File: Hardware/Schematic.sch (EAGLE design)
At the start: 14 parts, among them IC1 XC6220A331MR-G, J1 SAMACSYS_PARTS_USB4110-GF-A, Q1 20V/4.2A/52mΩ/1.4W

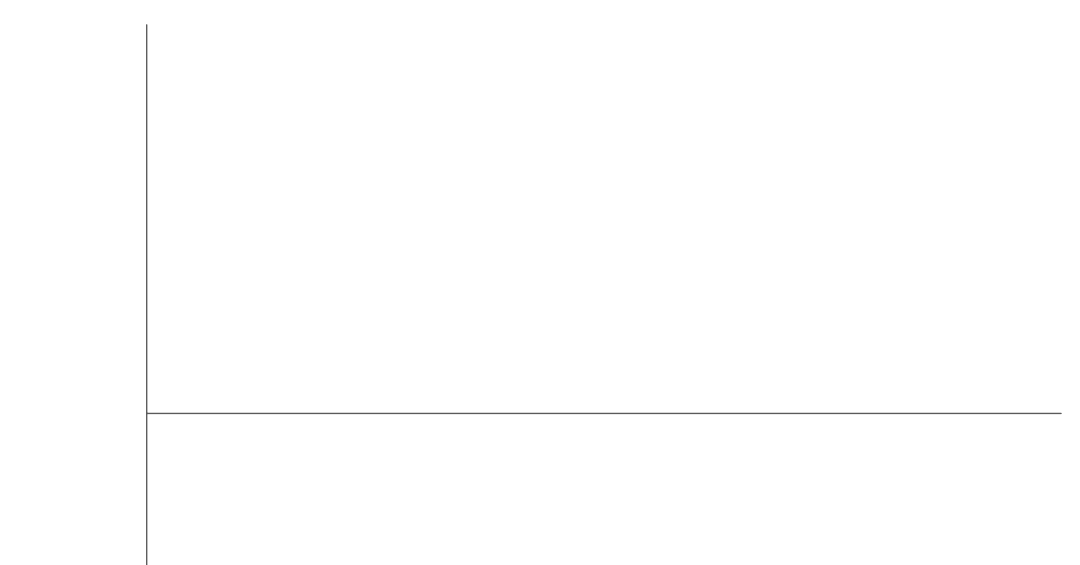
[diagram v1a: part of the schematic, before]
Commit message: add SD Card
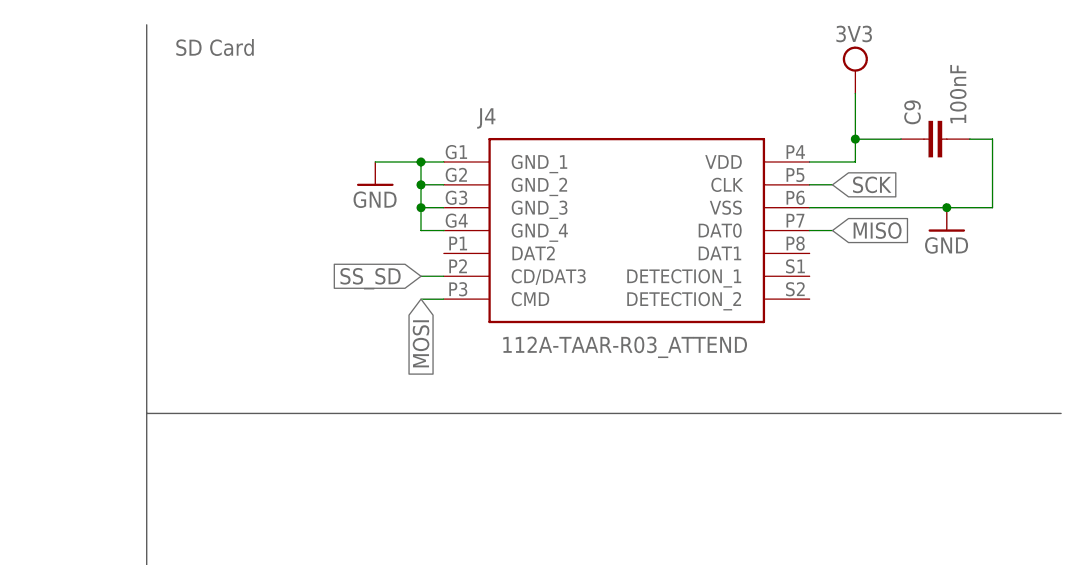
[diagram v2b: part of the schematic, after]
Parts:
- added C9: 100nF, DeskAssistant v19 v1.flbr:EAGLE-LTSPICE_CC0402
- added J4: 112A-TAAR-R03_ATTEND, DeskAssistant v19 v1.flbr:112A-TAAR-R03_ATTEND
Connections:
- new net MISO: J4.DAT0
- new net MOSI: J4.CMD
- new net SCK: J4.CLK
- new net SS_SD: J4.CD/DAT3
- net 3V3: now also C9.1, J4.VDD
- net GND: now also C9.2, J4.GND_1, J4.GND_2, J4.GND_3, J4.GND_4, J4.VSS
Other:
- note added: "SD Card"
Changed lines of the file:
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@@
 <part name="C1_BAT2" library="DeskAssistant v19 v1.flbr" library_urn="urn:adsk.wipprod:fs.file:vf.vVvdDOfaSfavM5thX5SjWw" deviceset="ESP32_WROVER_EAGLE-LTSPICE_C" device="C0402" value="4.7uF"/>
 <part name="C1_BAT1" library="DeskAssistant v19 v1.flbr" library_urn="urn:adsk.wipprod:fs.file:vf.vVvdDOfaSfavM5thX5SjWw" deviceset="ESP32_WROVER_EAGLE-LTSPICE_C" device="C0402" value="4.7uF"/>
+<part name="J4" library="DeskAssistant v19 v1.flbr" library_urn="urn:adsk.wipprod:fs.file:vf.vVvdDOfaSfavM5thX5SjWw" deviceset="112A-TAAR-R03_ATTEND" device=""/>
+<part name="GND11" library="DeskAssistant v19 v1.flbr" library_urn="urn:adsk.wipprod:fs.file:vf.vVvdDOfaSfavM5thX5SjWw" deviceset="GND" device=""/>
+<part name="GND12" library="DeskAssistant v19 v1.flbr" library_urn="urn:adsk.wipprod:fs.file:vf.vVvdDOfaSfavM5thX5SjWw" deviceset="GND" device=""/>
+<part name="C9" library="DeskAssistant v19 v1.flbr" library_urn="urn:adsk.wipprod:fs.file:vf.vVvdDOfaSfavM5thX5SjWw" deviceset="EAGLE-LTSPICE_C" device="C0402" value="100nF"/>
+<part name="SUPPLY2" library="DeskAssistant v19 v1.flbr" library_urn="urn:adsk.wipprod:fs.file:vf.vVvdDOfaSfavM5thX5SjWw" deviceset="3V3-CIRCLE" device="" value="3V3"/>
 </parts>
 <sheets>
@@
 ESD Protection</text>
 <text x="-2.54" y="271.78" size="1.778" layer="95" align="center">LDO Voltage Regulator</text>
+<text x="124.46" y="274.32" size="1.778" layer="95" align="center">SD Card</text>
 </plain>
 <instances>
@@
 <attribute name="NAME" x="23.876" y="235.839" size="1.778" layer="95" rot="R180"/>
 <attribute name="VALUE" x="23.876" y="240.919" size="1.778" layer="96" rot="R180"/>
+</instance>
+<instance part="J4" gate="G$1" x="149.86" y="261.62" smashed="yes">
+<attribute name="NAME" x="153.67" y="266.7" size="1.778" layer="95" align="center-left"/>
+<attribute name="VALUE" x="156.21" y="241.3" size="1.778" layer="96" align="center-left"/>
+</instance>
+<instance part="GND11" gate="1" x="142.24" y="259.08" smashed="yes">
+<attribute name="VALUE" x="139.7" y="256.54" size="1.778" layer="96"/>
+</instance>
+<instance part="GND12" gate="1" x="205.74" y="254" smashed="yes">
+<attribute name="VALUE" x="203.2" y="251.46" size="1.778" layer="96"/>
+</instance>
+<instance part="C9" gate="G$1" x="203.2" y="264.16" smashed="yes" rot="R90">
+<attribute name="NAME" x="202.819" y="265.684" size="1.778" layer="95" rot="R90"/>
+<attribute name="VALUE" x="207.899" y="265.684" size="1.778" layer="96" rot="R90"/>
+</instance>
+<instance part="SUPPLY2" gate="G$1" x="195.58" y="271.78" smashed="yes">
+<attribute name="VALUE" x="195.453" y="274.955" size="1.778" layer="96" align="bottom-center"/>
 </instance>
 </instances>
@@
 <pinref part="GND10" gate="1" pin="GND"/>
 </segment>
+<segment>
+<pinref part="J4" gate="G$1" pin="GND_4"/>
+<wire x1="149.86" y1="254" x2="147.32" y2="254" width="0.1524" layer="91"/>
+<wire x1="147.32" y1="254" x2="147.32" y2="256.54" width="0.1524" layer="91"/>
+<wire x1="147.32" y1="256.54" x2="147.32" y2="259.08" width="0.1524" layer="91"/>
+<wire x1="147.32" y1="259.08" x2="147.32" y2="261.62" width="0.1524" layer="91"/>
+<wire x1="147.32" y1="261.62" x2="149.86" y2="261.62" width="0.1524" layer="91"/>
+<pinref part="J4" gate="G$1" pin="GND_1"/>
+<pinref part="J4" gate="G$1" pin="GND_2"/>
+<wire x1="149.86" y1="259.08" x2="147.32" y2="259.08" width="0.1524" layer="91"/>
+<junction x="147.32" y="259.08"/>
+<pinref part="J4" gate="G$1" pin="GND_3"/>
+<wire x1="149.86" y1="256.54" x2="147.32" y2="256.54" width="0.1524" layer="91"/>
+<junction x="147.32" y="256.54"/>
+<wire x1="147.32" y1="261.62" x2="142.24" y2="261.62" width="0.1524" layer="91"/>
+<junction x="147.32" y="261.62"/>
+<pinref part="GND11" gate="1" pin="GND"/>
+</segment>
+<segment>
+<pinref part="J4" gate="G$1" pin="VSS"/>
+<wire x1="190.5" y1="256.54" x2="205.74" y2="256.54" width="0.1524" layer="91"/>
+<pinref part="GND12" gate="1" pin="GND"/>
+<pinref part="C9" gate="G$1" pin="2"/>
+<wire x1="208.28" y1="264.16" x2="210.82" y2="264.16" width="0.1524" layer="91"/>
+<wire x1="210.82" y1="264.16" x2="210.82" y2="256.54" width="0.1524" layer="91"/>
+<wire x1="210.82" y1="256.54" x2="205.74" y2="256.54" width="0.1524" layer="91"/>
+<junction x="205.74" y="256.54"/>
+</segment>
 </net>
 <net name="VUSB" class="0">
@@
 <wire x1="78.74" y1="246.38" x2="78.74" y2="241.3" width="0.1524" layer="91"/>
 <pinref part="C1_BAT2" gate="G$1" pin="2"/>
+</segment>
+<segment>
+<pinref part="J4" gate="G$1" pin="VDD"/>
+<wire x1="190.5" y1="261.62" x2="195.58" y2="261.62" width="0.1524" layer="91"/>
+<wire x1="195.58" y1="261.62" x2="195.58" y2="264.16" width="0.1524" layer="91"/>
+<wire x1="195.58" y1="264.16" x2="200.66" y2="264.16" width="0.1524" layer="91"/>
+<pinref part="C9" gate="G$1" pin="1"/>
+<wire x1="195.58" y1="264.16" x2="195.58" y2="269.24" width="0.1524" layer="91"/>
+<junction x="195.58" y="264.16"/>
+<pinref part="SUPPLY2" gate="G$1" pin="3V3"/>
 </segment>
 </net>
@@
 </segment>
 </net>
+<net name="SS_SD" class="0">
+<segment>
+<pinref part="J4" gate="G$1" pin="CD/DAT3"/>
+<wire x1="149.86" y1="248.92" x2="147.32" y2="248.92" width="0.1524" layer="91"/>
+<label x="147.32" y="248.92" size="1.778" layer="95" rot="R180" xref="yes"/>
+</segment>
+</net>
+<net name="MOSI" class="0">
+<segment>
+<pinref part="J4" gate="G$1" pin="CMD"/>
+<wire x1="149.86" y1="246.38" x2="147.32" y2="246.38" width="0.1524" layer="91"/>
+<label x="147.32" y="246.38" size="1.778" layer="95" rot="R270" xref="yes"/>
+</segment>
+</net>
+<net name="MISO" class="0">
+<segment>
+<pinref part="J4" gate="G$1" pin="DAT0"/>
+<wire x1="190.5" y1="254" x2="193.04" y2="254" width="0.1524" layer="91"/>
+<label x="193.04" y="254" size="1.778" layer="95" xref="yes"/>
+</segment>
+</net>
+<net name="SCK" class="0">
+<segment>
+<pinref part="J4" gate="G$1" pin="CLK"/>
+<wire x1="190.5" y1="259.08" x2="193.04" y2="259.08" width="0.1524" layer="91"/>
+<label x="193.04" y="259.08" size="1.778" layer="95" xref="yes"/>
+</segment>
+</net>

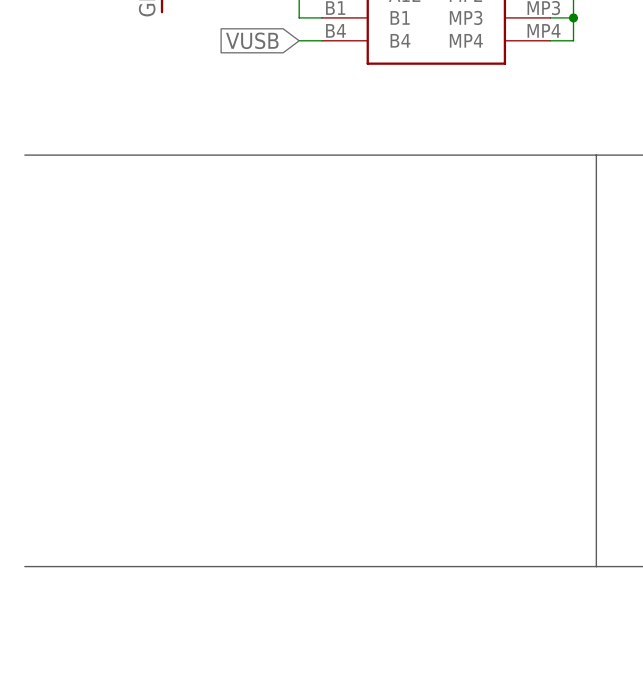
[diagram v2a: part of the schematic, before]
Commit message: add display type selector
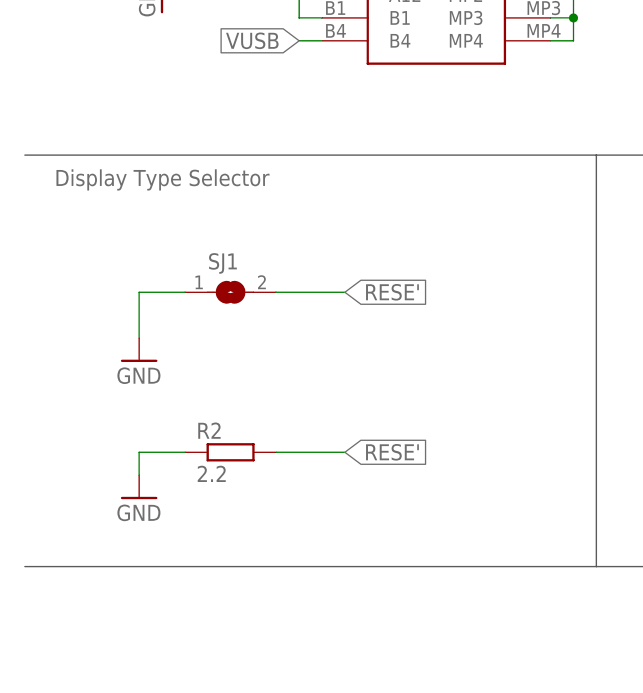
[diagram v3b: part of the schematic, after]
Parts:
- added R2: 2.2, DeskAssistant v19 v1.flbr:ESP32_WROVER_EAGLE-LTSPICE_RR0402
- added SJ1: (no value), DeskAssistant v19 v1.flbr:SJ
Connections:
- new net RESE': R2.2, SJ1.2
- net GND: now also R2.1, SJ1.1
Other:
- note added: "Display Type Selector"
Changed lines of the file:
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@@
 <part name="C9" library="DeskAssistant v19 v1.flbr" library_urn="urn:adsk.wipprod:fs.file:vf.vVvdDOfaSfavM5thX5SjWw" deviceset="EAGLE-LTSPICE_C" device="C0402" value="100nF"/>
 <part name="SUPPLY2" library="DeskAssistant v19 v1.flbr" library_urn="urn:adsk.wipprod:fs.file:vf.vVvdDOfaSfavM5thX5SjWw" deviceset="3V3-CIRCLE" device="" value="3V3"/>
+<part name="R2" library="DeskAssistant v19 v1.flbr" library_urn="urn:adsk.wipprod:fs.file:vf.vVvdDOfaSfavM5thX5SjWw" deviceset="ESP32_WROVER_EAGLE-LTSPICE_R" device="R0402" value="2.2"/>
+<part name="SJ1" library="DeskAssistant v19 v1.flbr" library_urn="urn:adsk.wipprod:fs.file:vf.vVvdDOfaSfavM5thX5SjWw" deviceset="SJ" device=""/>
+<part name="GND13" library="DeskAssistant v19 v1.flbr" library_urn="urn:adsk.wipprod:fs.file:vf.vVvdDOfaSfavM5thX5SjWw" deviceset="GND" device=""/>
+<part name="GND14" library="DeskAssistant v19 v1.flbr" library_urn="urn:adsk.wipprod:fs.file:vf.vVvdDOfaSfavM5thX5SjWw" deviceset="GND" device=""/>
 </parts>
 <sheets>
@@
 <text x="-2.54" y="271.78" size="1.778" layer="95" align="center">LDO Voltage Regulator</text>
 <text x="124.46" y="274.32" size="1.778" layer="95" align="center">SD Card</text>
+<text x="-147.32" y="210.82" size="1.778" layer="95" align="center">Display Type Selector</text>
 </plain>
 <instances>
@@
 <instance part="SUPPLY2" gate="G$1" x="195.58" y="271.78" smashed="yes">
 <attribute name="VALUE" x="195.453" y="274.955" size="1.778" layer="96" align="bottom-center"/>
+</instance>
+<instance part="R2" gate="G$1" x="-139.7" y="180.34" smashed="yes">
+<attribute name="NAME" x="-143.51" y="181.8386" size="1.778" layer="95"/>
+<attribute name="VALUE" x="-143.51" y="177.038" size="1.778" layer="96"/>
+<attribute name="NAME" x="-143.51" y="181.8386" size="1.778" layer="95"/>
+<attribute name="VALUE" x="-143.51" y="177.038" size="1.778" layer="96"/>
+</instance>
+<instance part="SJ1" gate="1" x="-139.7" y="198.12" smashed="yes">
+<attribute name="NAME" x="-142.24" y="200.66" size="1.778" layer="95"/>
+<attribute name="VALUE" x="-142.24" y="194.31" size="1.778" layer="96"/>
+</instance>
+<instance part="GND13" gate="1" x="-149.86" y="190.5" smashed="yes">
+<attribute name="VALUE" x="-152.4" y="187.96" size="1.778" layer="96"/>
+</instance>
+<instance part="GND14" gate="1" x="-149.86" y="175.26" smashed="yes">
+<attribute name="VALUE" x="-152.4" y="172.72" size="1.778" layer="96"/>
 </instance>
 </instances>
@@
 <junction x="205.74" y="256.54"/>
 </segment>
+<segment>
+<pinref part="SJ1" gate="1" pin="1"/>
+<wire x1="-144.78" y1="198.12" x2="-149.86" y2="198.12" width="0.1524" layer="91"/>
+<wire x1="-149.86" y1="198.12" x2="-149.86" y2="193.04" width="0.1524" layer="91"/>
+<pinref part="GND13" gate="1" pin="GND"/>
+</segment>
+<segment>
+<pinref part="R2" gate="G$1" pin="1"/>
+<wire x1="-144.78" y1="180.34" x2="-149.86" y2="180.34" width="0.1524" layer="91"/>
+<wire x1="-149.86" y1="180.34" x2="-149.86" y2="177.8" width="0.1524" layer="91"/>
+<pinref part="GND14" gate="1" pin="GND"/>
+</segment>
 </net>
 <net name="VUSB" class="0">
@@
 </segment>
 </net>
+<net name="RESE'" class="0">
+<segment>
+<pinref part="SJ1" gate="1" pin="2"/>
+<wire x1="-134.62" y1="198.12" x2="-127" y2="198.12" width="0.1524" layer="91"/>
+<label x="-127" y="198.12" size="1.778" layer="95" xref="yes"/>
+</segment>
+<segment>
+<pinref part="R2" gate="G$1" pin="2"/>
+<wire x1="-134.62" y1="180.34" x2="-127" y2="180.34" width="0.1524" layer="91"/>
+<label x="-127" y="180.34" size="1.778" layer="95" xref="yes"/>
+</segment>
+</net>

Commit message: E-Paper Drive Circuit
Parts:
- added C1: 4.7uF/25V, DeskAssistant v19 v1.flbr:EAGLE-LTSPICE_CC0402
- added C7: 10uF, DeskAssistant v19 v1.flbr:EAGLE-LTSPICE_CC0402
- added D3, D4, D5: MBR0530, DeskAssistant v19 v1.flbr:MBR0530
- added L1: 68uH, DeskAssistant v19 v1.flbr:744043680IND_4828-WE-TPC_WRE
- added Q2: SI1308EDL-T1-GE3, DeskAssistant v19 v1.flbr:SI1308EDL-T1-GE3
- added R1: 0.47, DeskAssistant v19 v1.flbr:ESP32_WROVER_EAGLE-LTSPICE_RR0402
- added R4: 10K, DeskAssistant v19 v1.flbr:ESP32_WROVER_EAGLE-LTSPICE_RR0402
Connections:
- new net EPD_3V3: C7.1, L1.2
- new net GDR: Q2.G, R4.2
- new net N$4: C1.1, D3.K, D4.A
- new net PREVGH: D5.A
- new net PREVGL: D3.A
- new net RESE: Q2.S, R1.1
- new net SRC: C1.2, D5.K, L1.1, Q2.D
- net GND: now also C7.2, D4.K, R4.1
- net RESE': now also R1.2
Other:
- note added: "E-Paper Drive Circuit"
